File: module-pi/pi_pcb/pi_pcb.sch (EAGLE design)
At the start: 8 parts, among them IC3 PIC16F870SO, K1 PIN20X2

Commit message: First pi hat PCB submitted.
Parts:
- removed IC3: PIC16F870SO, microchip:PIC16F870SO
- added JP5, JP6: (no value), pinhead:PINHD-2X4
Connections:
- new net +12V: IC2.14, JP1.2, JP5.2, JP6.2
- new net 0V: IC2.18, JP1.6, JP1.8
- new net GPIO13: JP6.5, K1.33
- new net GPIO6: JP5.5, K1.31
- new net ICSP_MCLR: IC2.1, JP4.1
- new net ICSP_PGC: IC2.5, JP4.5
- new net ICSP_PGD: IC2.4, JP4.4
- new net N$6: JP4.6
- new net STROBE+: JP1.7, JP1.9
- new net STROBE+_RES: IC2.15, JP1.5
- new net STROBE-: IC2.17, JP1.10
- new net STROBE_GATE: IC2.19
- new net STROBE_TRIG_IN: IC2.20, K1.29
- net +3V3: now also IC2.2, IC2.24, JP1.1, JP4.2, JP5.1, JP6.1
- net +5V: now also IC2.13, JP1.4, JP5.4, JP6.4
- net CE0: now also IC2.22
- net GND: now also IC2.23, IC2.3, JP1.3, JP4.3, JP5.3, JP6.3
- net MISO: now also IC2.28, JP5.8, JP6.8
- net MOSI: now also IC2.27, JP5.6, JP6.6
- net SCLK: now also IC2.26, JP5.7, JP6.7
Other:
- moved on the sheet: IC1, IC2, JP1, JP2, JP3, JP4

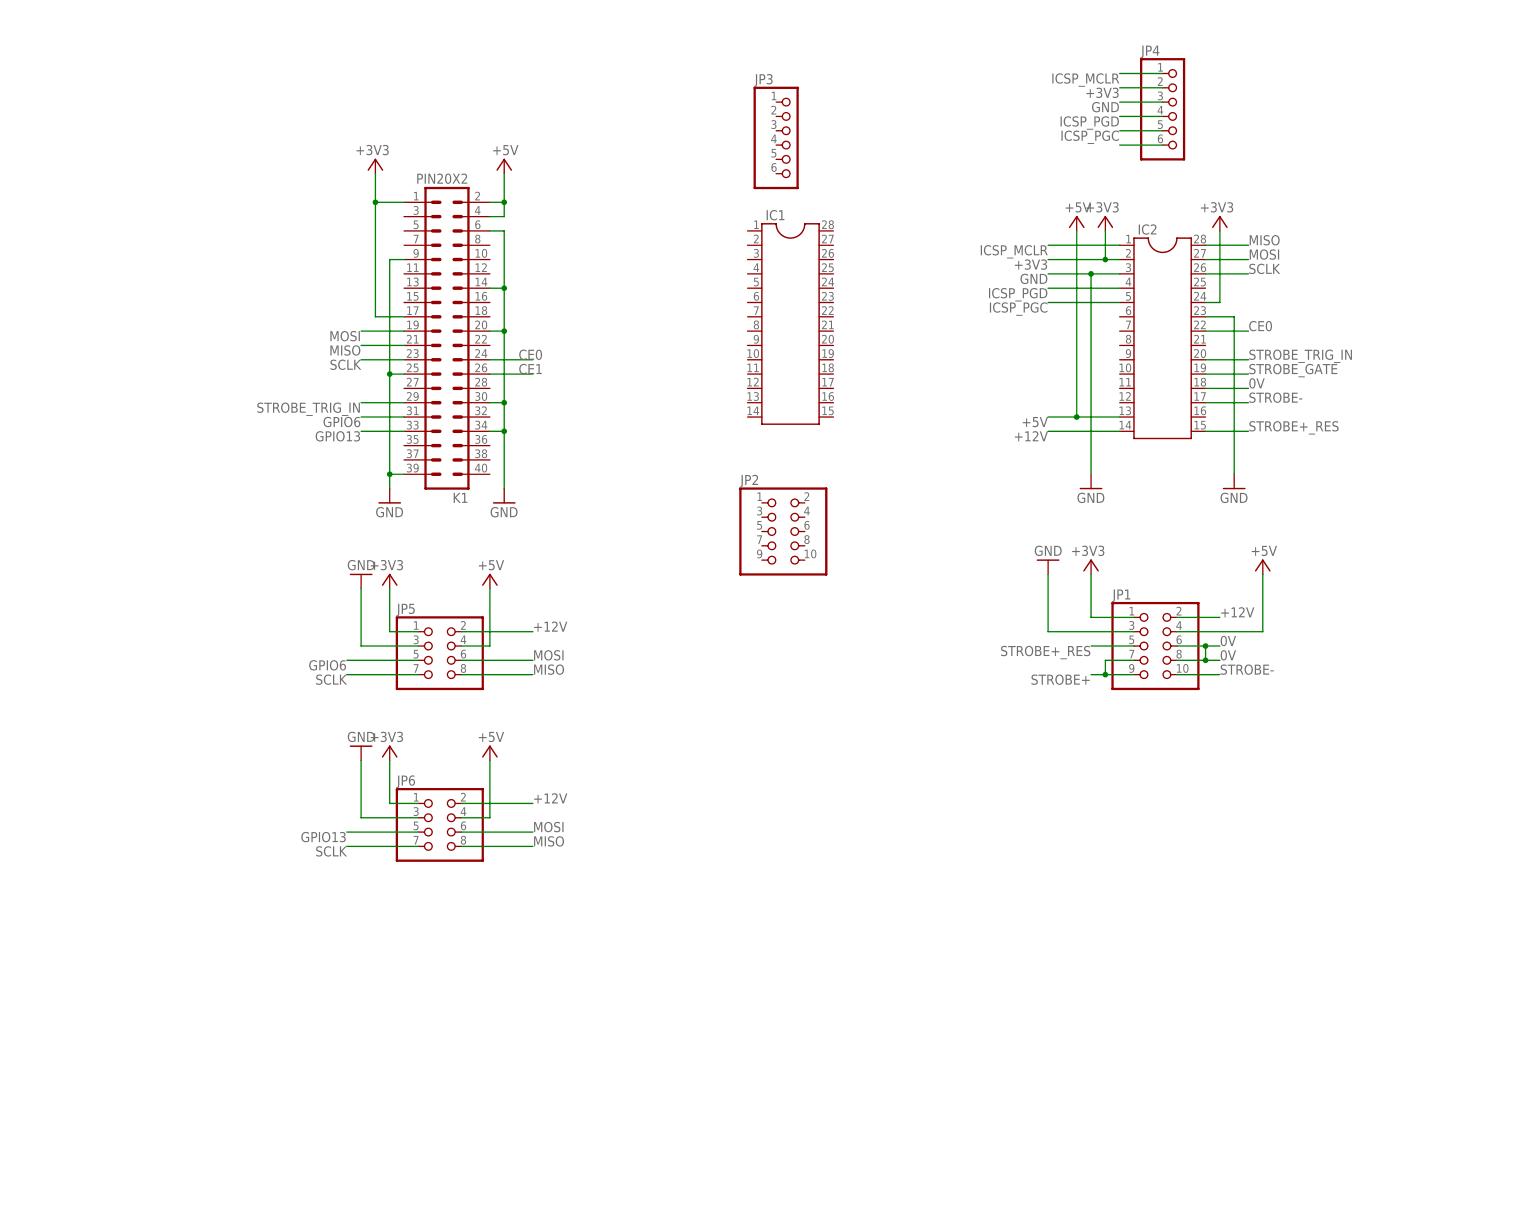
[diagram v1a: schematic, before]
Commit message: Express order with 4-layer pressure/flow board.
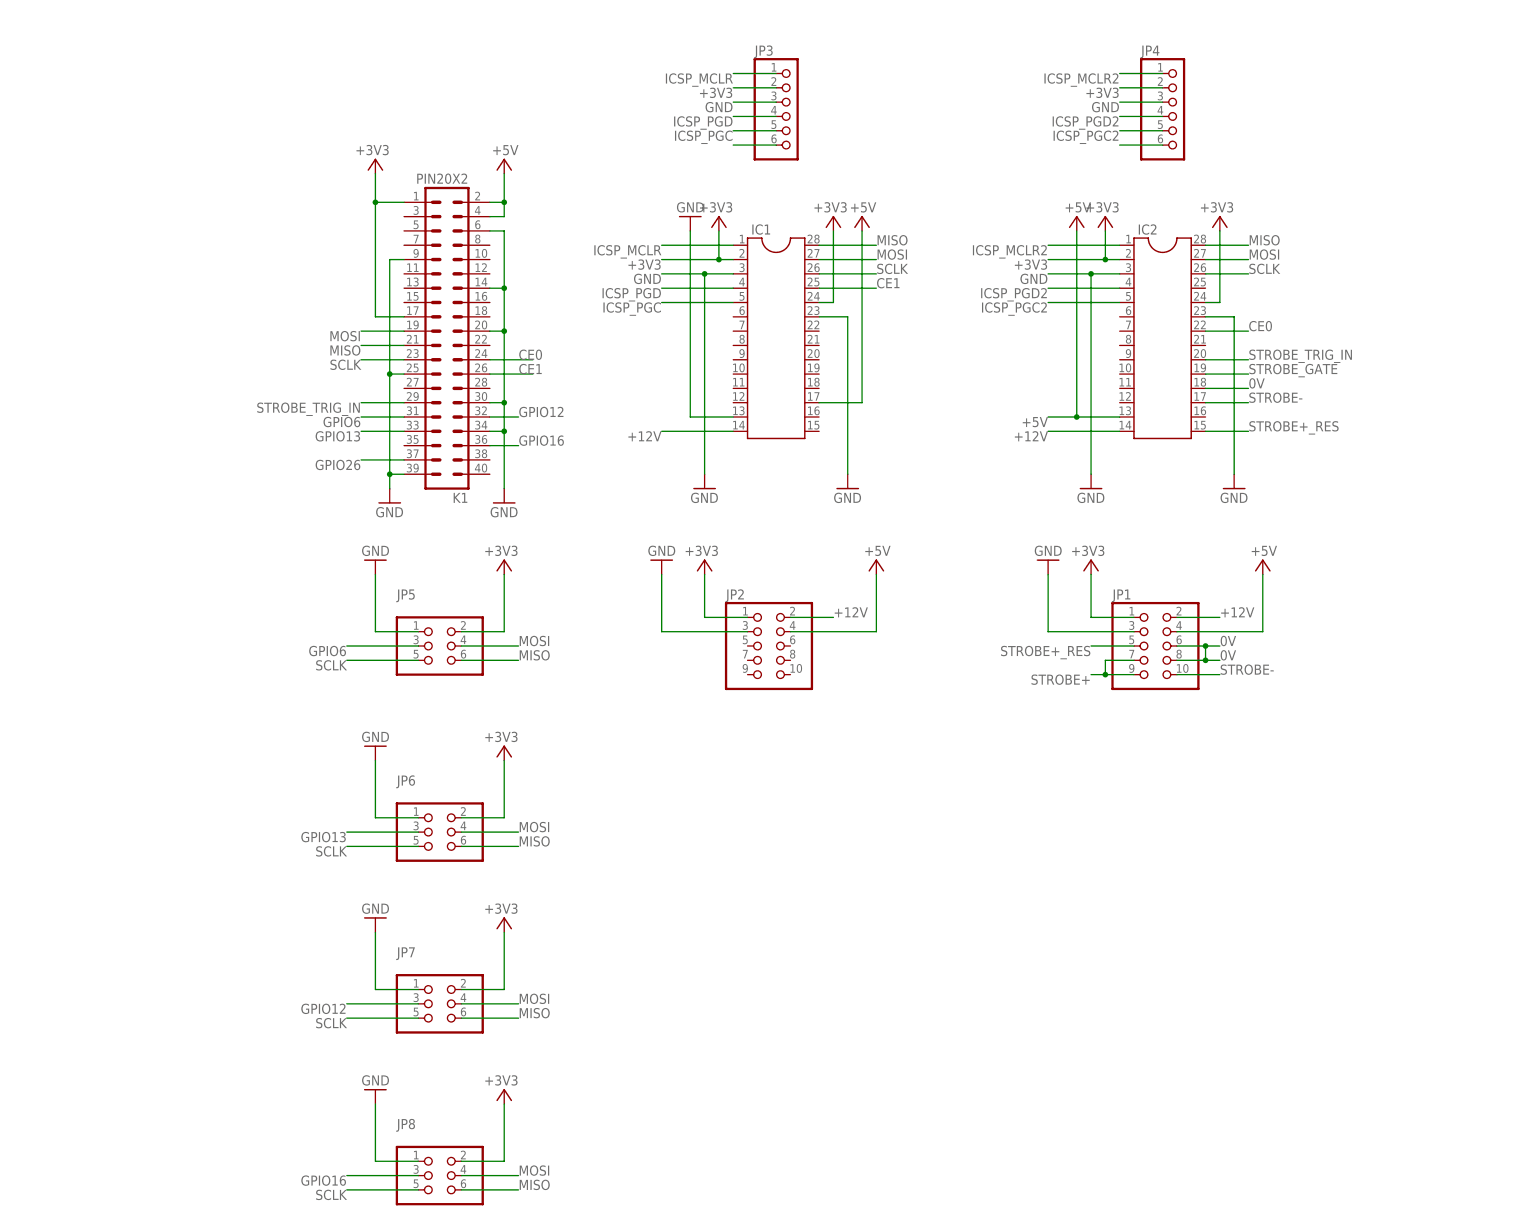
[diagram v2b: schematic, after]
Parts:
- added JP7, JP8: (no value), pinhead:PINHD-2X3
- JP5, JP6: device pinhead:PINHD-2X4 -> pinhead:PINHD-2X3
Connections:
- new net GPIO12: JP7.3, K1.32
- new net GPIO16: JP8.3, K1.36
- new net GPIO26: K1.37
- new net ICSP_MCLR2: IC2.1, JP4.1
- new net ICSP_PGC2: IC2.5, JP4.5
- new net ICSP_PGD2: IC2.4, JP4.4
- new net N$1: JP3.6
- net +12V: now also IC1.14, JP2.2; no longer JP5.2, JP6.2
- net +3V3: now also IC1.2, IC1.24, JP2.1, JP3.2, JP5.2, JP6.2, JP7.2, JP8.2; no longer JP5.1, JP6.1
- net +5V: now also IC1.17, JP2.4; no longer JP5.4, JP6.4
- net CE1: now also IC1.25
- net GND: now also IC1.13, IC1.23, IC1.3, JP2.3, JP3.3, JP5.1, JP6.1, JP7.1, JP8.1; no longer JP5.3, JP6.3
- net GPIO13: now also JP6.3; no longer JP6.5
- net GPIO6: now also JP5.3; no longer JP5.5
- net ICSP_MCLR: now also IC1.1, JP3.1; no longer IC2.1, JP4.1
- net ICSP_PGC: now also IC1.5, JP3.5; no longer IC2.5, JP4.5
- net ICSP_PGD: now also IC1.4, JP3.4; no longer IC2.4, JP4.4
- net MISO: now also IC1.28, JP5.6, JP6.6, JP7.6, JP8.6; no longer JP5.8, JP6.8
- net MOSI: now also IC1.27, JP5.4, JP6.4, JP7.4, JP8.4; no longer JP5.6, JP6.6
- net SCLK: now also IC1.26, JP5.5, JP6.5, JP7.5, JP8.5; no longer JP5.7, JP6.7
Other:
- moved on the sheet: IC1, JP2, JP3

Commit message: Module headers replaced.
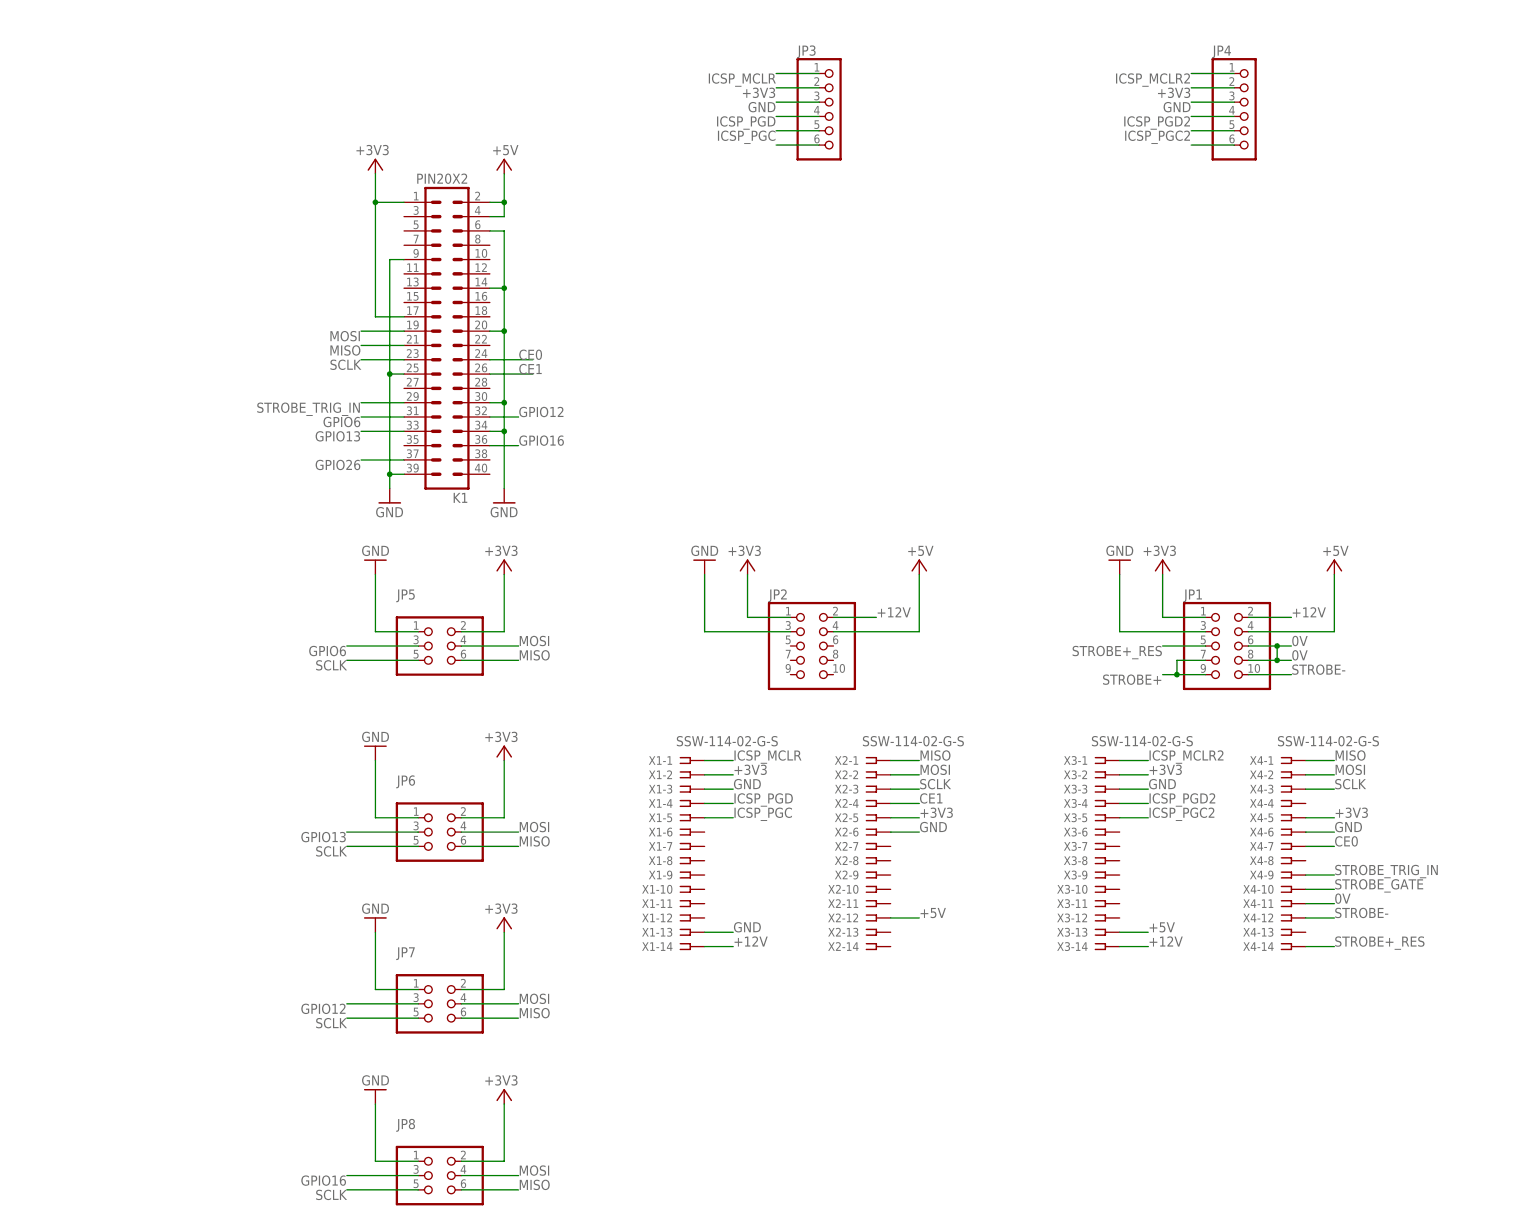
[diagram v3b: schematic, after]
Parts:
- removed IC1, IC2: (no value), ic-package:DIL28
- added X1, X2, X3, X4: SSW-114-02-G-S, con-samtec:SSW-114-02-G-S
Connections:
- net +12V: now also X1-14.1, X3-14.1; no longer IC1.14, IC2.14
- net +3V3: now also X1-2.1, X2-5.1, X3-2.1, X4-5.1; no longer IC1.2, IC1.24, IC2.2, IC2.24
- net +5V: now also X2-12.1, X3-13.1; no longer IC1.17, IC2.13
- net 0V: now also X4-11.1; no longer IC2.18
- net CE0: now also X4-7.1; no longer IC2.22
- net CE1: now also X2-4.1; no longer IC1.25
- net GND: now also X1-13.1, X1-3.1, X2-6.1, X3-3.1, X4-6.1; no longer IC1.13, IC1.23, IC1.3, IC2.23, IC2.3
- net ICSP_MCLR: now also X1-1.1; no longer IC1.1
- net ICSP_MCLR2: now also X3-1.1; no longer IC2.1
- net ICSP_PGC: now also X1-5.1; no longer IC1.5
- net ICSP_PGC2: now also X3-5.1; no longer IC2.5
- net ICSP_PGD: now also X1-4.1; no longer IC1.4
- net ICSP_PGD2: now also X3-4.1; no longer IC2.4
- net MISO: now also X2-1.1, X4-1.1; no longer IC1.28, IC2.28
- net MOSI: now also X2-2.1, X4-2.1; no longer IC1.27, IC2.27
- net SCLK: now also X2-3.1, X4-3.1; no longer IC1.26, IC2.26
- net STROBE+_RES: now also X4-14.1; no longer IC2.15
- net STROBE-: now also X4-12.1; no longer IC2.17
- net STROBE_GATE: now also X4-10.1; no longer IC2.19
- net STROBE_TRIG_IN: now also X4-9.1; no longer IC2.20
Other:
- moved on the sheet: JP1, JP2, JP3, JP4

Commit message: Dedicated flow power 0V trace.
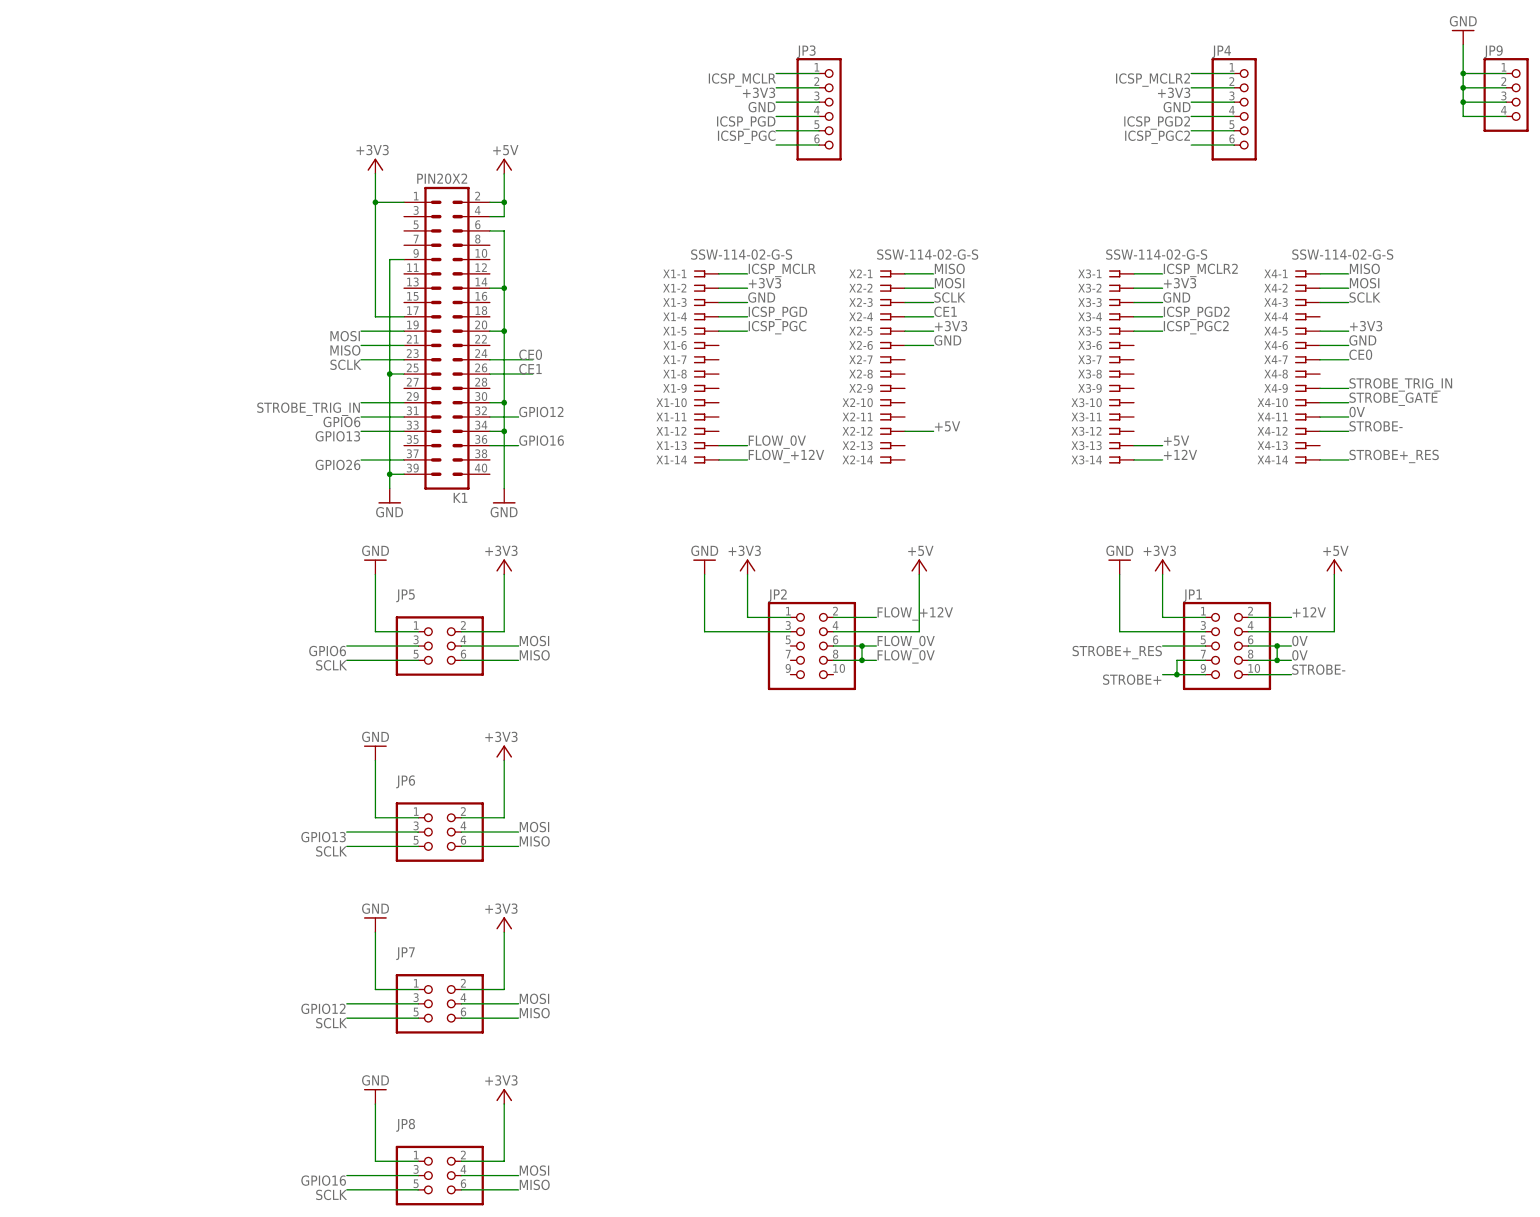
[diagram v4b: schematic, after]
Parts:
- added JP9: (no value), pinhead:PINHD-1X4
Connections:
- new net FLOW_+12V: JP2.2, X1-14.1
- new net FLOW_0V: JP2.6, JP2.8, X1-13.1
- net +12V: no longer JP2.2, X1-14.1
- net GND: now also JP9.1, JP9.2, JP9.3, JP9.4; no longer X1-13.1
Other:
- moved on the sheet: X1-1, X1-10, X1-11, X1-12, X1-13, X1-14, X1-2, X1-3, X1-4, X1-5, X1-6, X1-7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
